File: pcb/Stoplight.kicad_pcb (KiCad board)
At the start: 2 copper layers, 15 x 15 mm, 16 parts, among them IC1 ATtiny85-20M, IC2 AP7375-33SA-7

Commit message: Good double-sided design
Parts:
- R1, R2, R3, R4: footprint Resistor_SMD:R_0201_0603Metric -> Resistor_SMD:R_0603_1608Metric
- moved TP1 3.05 mm to (126.5, 84.7)
- moved R4 1.03 mm to (137.8, 86.2)
- moved R3 0.87 mm to (138.3, 88.0)
- moved R2 0.56 mm to (129.1, 83.5)
- moved R1 0.25 mm to (129.2, 82.0)
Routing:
- net +VBATT: track 7.02 -> 10.3 mm
- net SCK/A1: track 18.8 -> 20.5 mm
- net LED_G: track 3.88 -> 2.57 mm
- net LED_R: track 7.63 -> 6.57 mm
- net Net-(D1-A2): track 6.39 -> 5.50 mm
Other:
- outline, holes or cut-outs redrawn

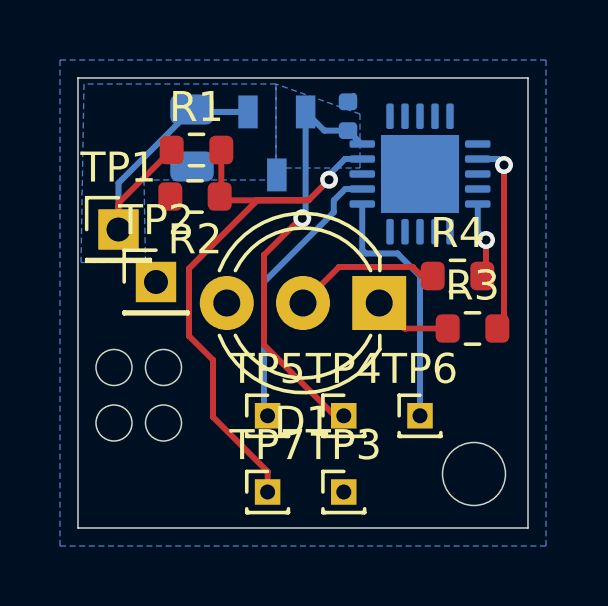
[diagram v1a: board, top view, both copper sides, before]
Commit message: Tested on breadboard, working
calibrated voltage levels
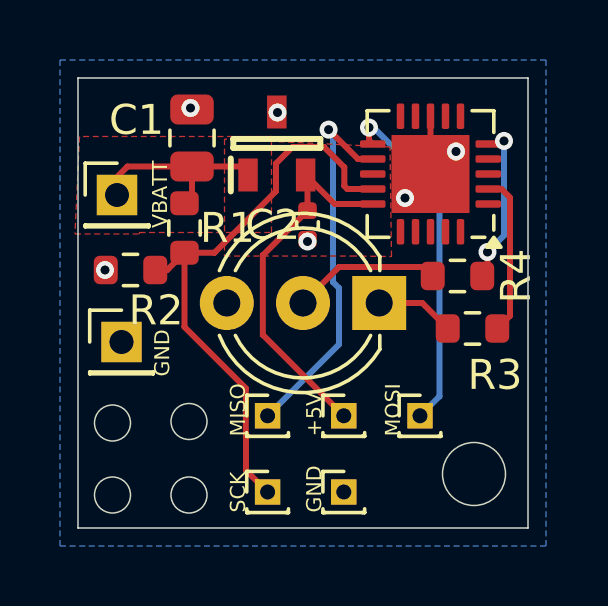
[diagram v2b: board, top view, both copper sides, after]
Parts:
- C1, C2, IC1, IC2: moved to F.Cu
- moved C2 3.87 mm to (132.8, 84.5), turned to 90 degrees
- moved R2 3.26 mm to (127.0, 86.0)
- moved R1 2.63 mm to (128.8, 84.6), turned to -90 degrees
- moved TP2 2.31 mm to (126.7, 88.4)
- moved TP1 1.15 mm to (126.5, 83.5)
- moved IC1 0.35 mm to (136.9, 82.8)
- turned C1 to -90 degrees
- turned IC2 to 90 degrees
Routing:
- net +VBATT: track 10.3 -> 6.64 mm
- net MISO: track 9.30 -> 12.5 mm, vias 0 -> 1
- net MOSI: track 8.47 -> 11.5 mm, vias 0 -> 1
- net LED_G: track 2.57 -> 5.37 mm, vias 1 -> 2
- net +5V: track 14.3 -> 12.4 mm, vias 1 -> 0
- net GND: track 0.45 -> 1.92 mm, vias 0 -> 6
- net LED_R: track 6.57 -> 5.38 mm, vias 1 -> 0
- net SCK/A1: track 20.5 -> 19.6 mm, vias 1 -> 0
- net Net-(D1-A2): track 5.50 -> 4.95 mm
- added copper zone on F.Cu, net +5V
- added copper zone on F.Cu, net +VBATT
- removed copper zone on B.Cu, net +5V
- removed copper zone on B.Cu, net +VBATT
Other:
- outline, holes or cut-outs redrawn
- board text added: "+5V"
- board text added: "GND"
- board text added: "MISO"
- board text added: "MOSI"
- board text added: "SCK"
- board text added: "VBATT"

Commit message: Another solid design, but going to try for even simpler
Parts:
- added POT1: TC33X-2-103E, digikey-footprints:Trimpot_3.8mmx3.6mm_TC33X-2-103E, B.Cu at (138.1, 83.8)
- added TP8: RST, Connector_PinHeader_1.00mm:PinHeader_1x01_P1.00mm_Vertical, F.Cu at (136.1, 93.5)
- moved TP4 3.07 mm to (131.0, 91.0)
- moved TP5 2.04 mm to (133.6, 91.0)
- moved R4 1.05 mm to (137.9, 87.2)
- moved R3 0.94 mm to (137.9, 88.8)
- moved TP1 0.80 mm to (126.5, 84.3)
- moved C1 0.55 mm to (129.6, 81.6)
- moved TP3 0.53 mm to (133.5, 93.5)
- moved TP7 0.53 mm to (131.0, 93.5)
- moved TP6 0.53 mm to (136.1, 91.0)
- moved R2 0.40 mm to (127.0, 86.4)
- moved IC2 0.32 mm to (132.2, 81.8)
- moved IC1 0.20 mm to (136.8, 82.8)
- moved R1 0.15 mm to (128.9, 84.6)
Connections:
- net SCK/A1 renamed SCK/BATT
- IC1 pad 11: MOSI -> MOSI/R
- IC1 pad 12: MISO -> MISO/G
- IC1 pad 2: LED_R -> DIM
- IC1 pad 5: LED_G -> unconnected-(IC1-XTAL2/PB4-Pad5)
- R3 pad 2: LED_R -> MOSI/R
- R4 pad 2: LED_G -> MISO/G
- TP5 pad 1: MISO -> MISO/G
- TP6 pad 1: MOSI -> MOSI/R
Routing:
- net MISO/G: track 0.00 -> 19.6 mm, vias 0 -> 1
- net MOSI/R: track 0.00 -> 16.0 mm, vias 0 -> 1
- net MISO: track 12.5 -> 0.00 mm, vias 1 -> 0
- net RST: track 0.00 -> 11.7 mm
- net MOSI: track 11.5 -> 0.00 mm, vias 1 -> 0
- net LED_R: track 5.38 -> 0.00 mm
- net LED_G: track 5.37 -> 0.00 mm, vias 2 -> 0
- net DIM: track 0.00 -> 3.18 mm, vias 0 -> 1
- net +5V: track 12.4 -> 14.1 mm, vias 0 -> 1
- net Net-(D1-A2): track 4.95 -> 5.85 mm
- net unconnected-(IC1-XTAL2/PB4-Pad5): track 0.00 -> 0.62 mm
- net SCK/BATT: track 19.6 -> 20.1 mm
- net GND: vias 6 -> 5
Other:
- outline, holes or cut-outs redrawn
- board text added: "RST"

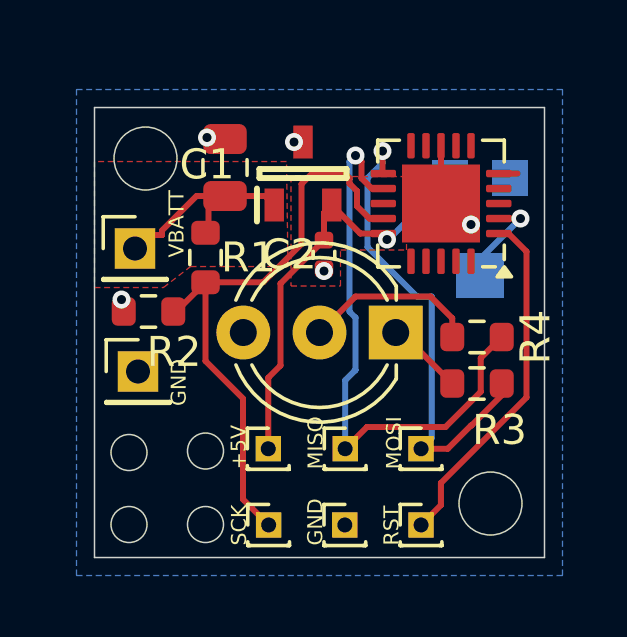
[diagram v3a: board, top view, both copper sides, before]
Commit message: Almost entirely single-layer now
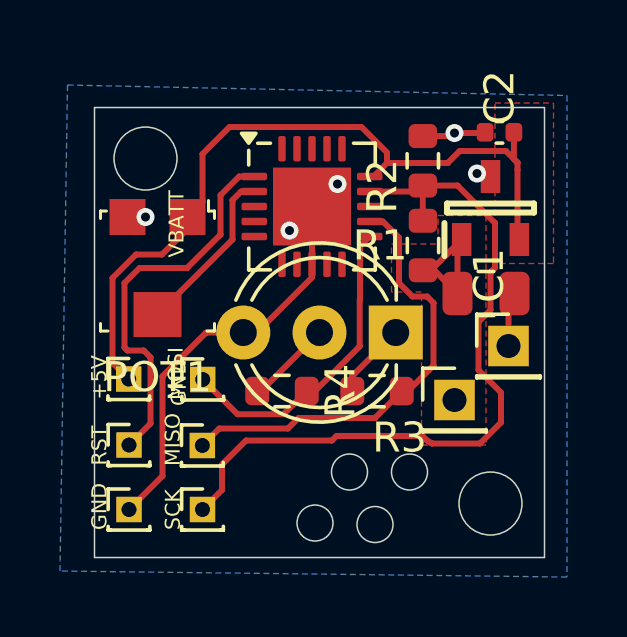
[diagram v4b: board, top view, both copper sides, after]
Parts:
- POT1: moved to F.Cu
- moved TP2 12.4 mm to (139.0, 87.5)
- moved TP1 11.8 mm to (137.2, 89.3)
- moved POT1 10.8 mm to (127.3, 85.0), turned to 180 degrees
- moved R2 10.4 mm to (136.1, 81.4), turned to 90 degrees
- moved TP8 10.1 mm to (126.3, 90.8)
- moved C1 9.66 mm to (138.2, 85.8), turned to 180 degrees
- moved TP6 7.63 mm to (128.8, 88.7)
- moved R1 7.26 mm to (136.2, 84.2), turned to 90 degrees
- moved TP3 7.21 mm to (126.3, 93.0)
- moved C2 7.13 mm to (138.7, 80.4), turned to 0 degrees
- moved R4 6.74 mm to (131.4, 89.0)
- moved IC2 6.35 mm to (138.4, 83.0)
- moved TP4 5.20 mm to (126.3, 88.7)
- moved TP5 4.76 mm to (128.8, 90.9)
- moved IC1 4.30 mm to (132.4, 82.9), turned to 0 degrees
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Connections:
- R3 pad 2: MOSI/R -> MISO/G
- R4 pad 2: MISO/G -> MOSI/R
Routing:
- net GND: track 1.92 -> 18.2 mm
- net +5V: track 14.1 -> 25.8 mm, vias 1 -> 0
- net MOSI/R: track 16.0 -> 10.6 mm, vias 1 -> 0
- net SCK/BATT: track 20.1 -> 25.0 mm
- net MISO/G: track 19.6 -> 15.0 mm, vias 1 -> 0
- net Net-(D1-A2): track 5.85 -> 2.88 mm
- net DIM: track 3.18 -> 5.69 mm, vias 1 -> 0
- net +VBATT: track 6.84 -> 5.04 mm
- net RST: track 11.7 -> 12.9 mm
- net unconnected-(IC1-XTAL2/PB4-Pad5): track 0.62 -> 0.00 mm
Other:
- outline, holes or cut-outs redrawn

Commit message: some rearranging
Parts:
- moved R3 0.25 mm to (134.6, 89.3)
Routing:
- net Net-(D1-A1): track 2.55 -> 2.80 mm, vias 0 -> 1
- net Net-(D1-A2): track 2.88 -> 2.98 mm, vias 0 -> 1
- net GND: vias 5 -> 6
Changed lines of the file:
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@@
 	(footprint "Resistor_SMD:R_0603_1608Metric"
 		(layer "F.Cu")
-		(at 134.618279 89.053269)
+		(at 134.618279 89.3)
 		(descr "Resistor SMD 0603 (1608 Metric), square (rectangular) end terminal, IPC_7351 nominal, (Body size source: IPC-SM-782 page 72, https://www.pcb-3d.com/wordpress/wp-content/uploads/ipc-sm-782a_amendment_1_and_2.pdf), generated with kicad-footprint-generator")
 		(tags "resistor")
@@
 	)
 	(segment
+		(start 131.664386 86.05)
+		(end 132.45 85.264386)
+		(width 0.2)
+		(layer "F.Cu")
+		(net 1)
+	)
+	(segment
 		(start 137.099196 80.550804)
 		(end 137.2 80.45)
@@
 	)
 	(segment
+		(start 131.6 86.05)
+		(end 131.664386 86.05)
+		(width 0.2)
+		(layer "F.Cu")
+		(net 1)
+	)
+	(segment
 		(start 139 86)
 		(end 139.2 85.8)
@@
 	(segment
 		(start 130.614386 87.1)
-		(end 132.45 85.264386)
+		(end 131.6 86.114386)
 		(width 0.2)
 		(layer "F.Cu")
@@
 	)
 	(segment
+		(start 131.6 86.114386)
+		(end 131.6 86.05)
+		(width 0.2)
+		(layer "F.Cu")
+		(net 1)
+	)
+	(segment
 		(start 138.19581 80.45)
 		(end 138.22 80.42581)
@@
 	)
 	(via
+		(at 131.6 86.05)
+		(size 0.6)
+		(drill 0.3)
+		(layers "F.Cu" "B.Cu")
+		(net 1)
+	)
+	(via
 		(at 126.9 83.25)
 		(size 0.6)
@@
 	)
 	(segment
-		(start 133.793279 89.053269)
-		(end 133.793279 88.546721)
+		(start 134.124265 88.324265)
+		(end 133.793279 88.655251)
 		(width 0.2)
 		(layer "F.Cu")
@@
 	)
 	(segment
-		(start 133.793279 88.546721)
+		(start 134.124265 88.215735)
 		(end 135.24 87.1)
 		(width 0.2)
@@
 	)
 	(segment
+		(start 133.793279 88.655251)
+		(end 133.793279 89.3)
+		(width 0.2)
+		(layer "F.Cu")
+		(net 18)
+	)
+	(segment
+		(start 134.124265 88.324265)
+		(end 134.124265 88.215735)
+		(width 0.2)
+		(layer "F.Cu")
+		(net 18)
+	)
+	(via
+		(at 134.124265 88.324265)
+		(size 0.6)
+		(drill 0.3)
+		(layers "F.Cu" "B.Cu")
+		(net 18)
+	)
+	(segment
+		(start 131.406141 88.558559)
+		(end 131.406141 88.393859)
+		(width 0.2)
+		(layer "F.Cu")
+		(net 19)
+	)
+	(segment
 		(start 130.75 89.05)
-		(end 132.7 87.1)
+		(end 130.625 89.05)
 		(width 0.2)
 		(layer "F.Cu")
@@
 	)
 	(segment
-		(start 130.625 89.05)
+		(start 131.241441 88.558559)
 		(end 130.75 89.05)
 		(width 0.2)
@@
 	)
 	(segment
+		(start 131.406141 88.393859)
+		(end 132.7 87.1)
+		(width 0.2)
+		(layer "F.Cu")
+		(net 19)
+	)
+	(segment
+		(start 131.406141 88.558559)
+		(end 131.241441 88.558559)
+		(width 0.2)
+		(layer "F.Cu")
+		(net 19)
+	)
+	(via
+		(at 131.406141 88.558559)
+		(size 0.6)
+		(drill 0.3)
+		(layers "F.Cu" "B.Cu")
+		(net 19)
+	)
+	(segment
 		(start 134.05 84.225)
 		(end 134.05 86)
@@
 	)
 	(segment
-		(start 134.814386 83.4)
-		(end 135.35 83.935614)
+		(start 135.35 85.45)
+		(end 135.8 85.9)
 		(width 0.2)
 		(layer "F.Cu")
@@
 	)
 	(segment
-		(start 129.36 90.3)
-		(end 131.65 90.3)
+		(start 128.795 90.865)
+		(end 129.36 90.3)
 		(width 0.2)
 		(layer "F.Cu")
@@
 	)
 	(segment
-		(start 136.5 88.2)
-		(end 135.646731 89.053269)
+		(start 129.36 90.3)
+		(end 131.65 90.3)
 		(width 0.2)
 		(layer "F.Cu")
@@
 	)
 	(segment
-		(start 131.65 90.3)
-		(end 132 89.95)
+		(start 135.443279 89.256721)
+		(end 135.443279 89.3)
 		(width 0.2)
 		(layer "F.Cu")
@@
 	)
 	(segment
-		(start 134.546548 89.95)
-		(end 135.443279 89.053269)
+		(start 134.643279 90.1)
+		(end 135.443279 89.3)
 		(width 0.2)
 		(layer "F.Cu")
@@
 	)
 	(segment
-		(start 134.375 83.4)
-		(end 134.814386 83.4)
+		(start 136.5 86.11)
+		(end 136.5 88.2)
 		(width 0.2)
 		(layer "F.Cu")
@@
 	)
 	(segment
-		(start 135.646731 89.053269)
-		(end 135.443279 89.053269)
+		(start 135.8 85.9)
+		(end 136.29 85.9)
 		(width 0.2)
 		(layer "F.Cu")
@@
 	)
 	(segment
-		(start 132 89.95)
-		(end 134.546548 89.95)
+		(start 131.65 90.3)
+		(end 131.85 90.1)
 		(width 0.2)
 		(layer "F.Cu")
@@
 	)
 	(segment
-		(start 128.795 90.865)
-		(end 129.36 90.3)
+		(start 136.5 88.2)
+		(end 135.443279 89.256721)
 		(width 0.2)
 		(layer "F.Cu")
@@
 	)
 	(segment
-		(start 135.8 85.9)
-		(end 136.29 85.9)
+		(start 134.814386 83.4)
+		(end 135.35 83.935614)
 		(width 0.2)
 		(layer "F.Cu")
@@
 	)
 	(segment
-		(start 136.5 86.11)
-		(end 136.5 88.2)
+		(start 131.85 90.1)
+		(end 134.643279 90.1)
 		(width 0.2)
 		(layer "F.Cu")
@@
 	)
 	(segment
-		(start 135.35 85.45)
-		(end 135.8 85.9)
+		(start 134.375 83.4)
+		(end 134.814386 83.4)
 		(width 0.2)
 		(layer "F.Cu")

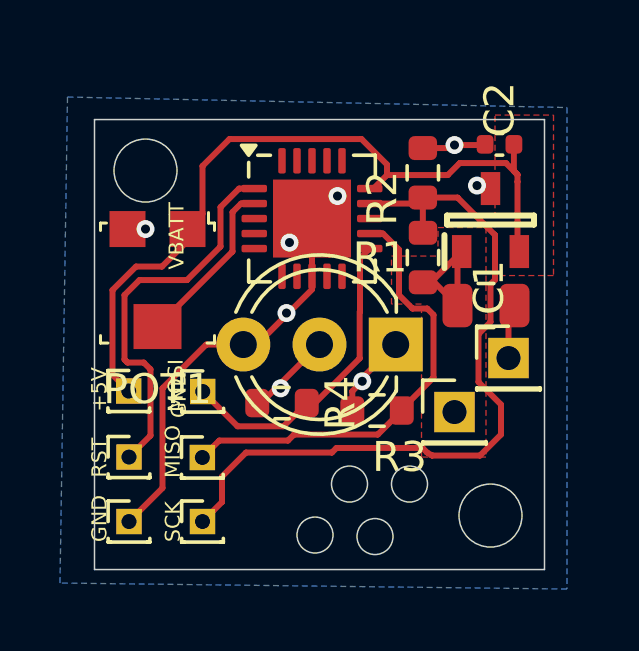
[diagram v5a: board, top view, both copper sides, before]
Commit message: Swapped mcu package to SOIC-8 for easier soldering
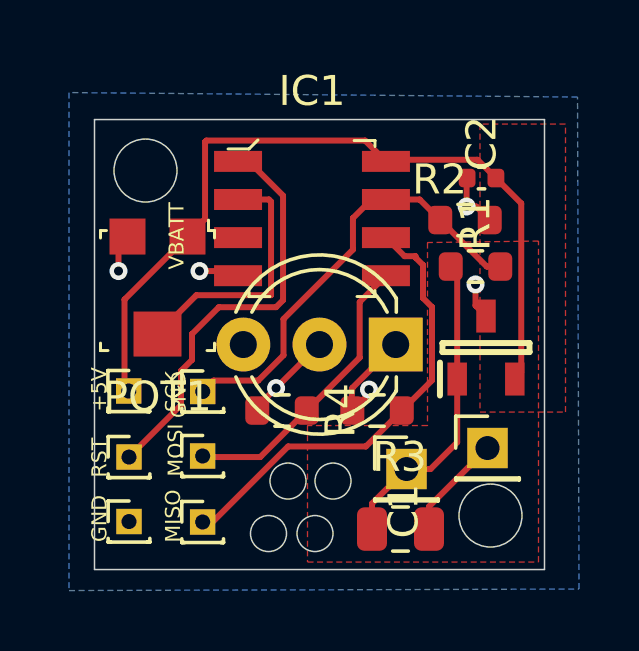
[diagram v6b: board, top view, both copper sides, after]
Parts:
- IC1: footprint Package_DFN_QFN:QFN-20-1EP_4x4mm_P0.5mm_EP2.6x2.6mm -> digikey-footprints:SOIC-8_W5.3mm
- R1: value 10K -> 10K .1%
- R2: value 3K3 -> 3K3 0.1%
- moved C1 7.98 mm to (135.4, 93.2)
- moved TP7 4.34 mm to (128.8, 88.7)
- moved IC2 4.25 mm to (138.2, 87.2)
- moved TP2 3.08 mm to (138.3, 90.5)
- moved TP1 2.48 mm to (135.6, 91.2)
- moved TP5 2.15 mm to (128.8, 93.0)
- moved TP6 2.15 mm to (128.8, 90.8)
- moved R2 2.11 mm to (137.6, 83.0), turned to 0 degrees
- moved R1 1.78 mm to (137.9, 84.5), turned to 0 degrees
- moved C2 1.27 mm to (138.1, 81.5)
- moved POT1 0.25 mm to (127.3, 85.3)
- moved R4 0.25 mm to (131.4, 89.3)
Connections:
- IC1 pad 4: unconnected-(IC1-NC-Pad4) -> GND
- IC1 pad 5: unconnected-(IC1-XTAL2/PB4-Pad5) -> MOSI/R
- IC1 pad 6: unconnected-(IC1-NC-Pad6) -> MISO/G
- IC1 pad 7: unconnected-(IC1-NC-Pad7) -> SCK/BATT
- IC1 pad 8: GND -> +5V
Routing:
- net SCK/BATT: track 25.0 -> 14.8 mm
- net GND: track 18.2 -> 9.24 mm, vias 6 -> 4
- net +VBATT: track 5.04 -> 10.5 mm
- net DIM: track 5.69 -> 8.57 mm
- net +5V: track 25.8 -> 26.9 mm
- net RST: track 12.9 -> 13.9 mm
- net Net-(D1-A1): track 2.80 -> 3.77 mm
- net MOSI/R: track 10.6 -> 9.72 mm
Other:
- outline, holes or cut-outs redrawn
